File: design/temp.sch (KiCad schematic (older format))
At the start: 2 parts, among them U301 LM73

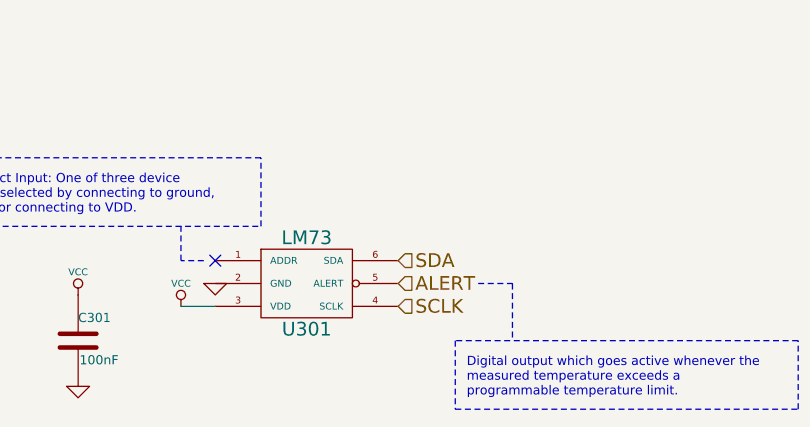
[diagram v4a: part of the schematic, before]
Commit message: Moved nRST cap closer to the MCU pin, connected crystal GND pins to the actual GND plane. Added several vias to GND and VDD planes.
Signed-off-by: Marcos Chaparro <marcos@mrkindustries.com.ar>
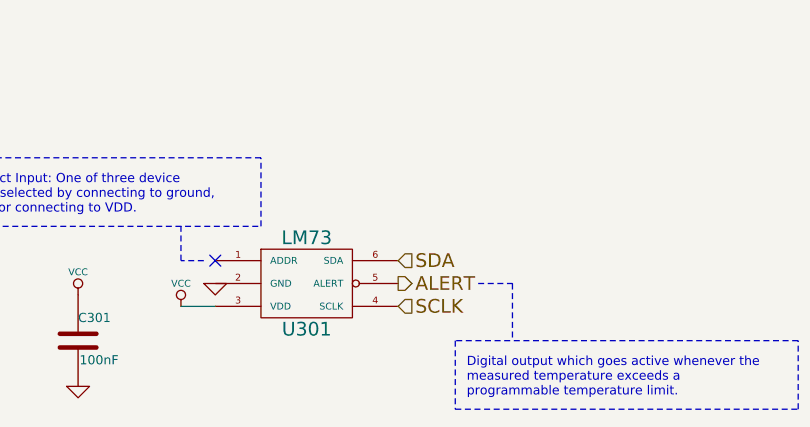
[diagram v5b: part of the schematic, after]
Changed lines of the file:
@@
 $EndComp
 $Comp
-L GND #PWR025
+L GND #PWR024
 U 1 1 53F5A7F7
 P 5400 3400
-F 0 "#PWR025" H 5400 3400 30  0001 C CNN
+F 0 "#PWR024" H 5400 3400 30  0001 C CNN
 F 1 "GND" H 5400 3330 30  0001 C CNN
 F 2 "" H 5400 3400 60  0000 C CNN
@@
 $EndComp
 $Comp
-L VCC #PWR026
+L VCC #PWR025
 U 1 1 53F5AB35
 P 5250 3500
-F 0 "#PWR026" H 5250 3600 30  0001 C CNN
+F 0 "#PWR025" H 5250 3600 30  0001 C CNN
 F 1 "VCC" H 5250 3600 30  0000 C CNN
 F 2 "" H 5250 3500 60  0001 C CNN
@@
 $EndComp
 $Comp
-L VCC #PWR027
+L VCC #PWR026
 U 1 1 53F5AB73
 P 4800 3450
-F 0 "#PWR027" H 4800 3550 30  0001 C CNN
+F 0 "#PWR026" H 4800 3550 30  0001 C CNN
 F 1 "VCC" H 4800 3550 30  0000 C CNN
 F 2 "" H 4800 3450 60  0001 C CNN
@@
 $EndComp
 $Comp
-L GND #PWR028
+L GND #PWR027
 U 1 1 53F5AB80
 P 4800 3850
-F 0 "#PWR028" H 4800 3850 30  0001 C CNN
+F 0 "#PWR027" H 4800 3850 30  0001 C CNN
 F 1 "GND" H 4800 3780 30  0001 C CNN
 F 2 "" H 4800 3850 60  0000 C CNN
@@
 Text HLabel 6200 3300 2    60   Input ~ 0
 SDA
-Text HLabel 6200 3400 2    60   Input ~ 0
+Text HLabel 6200 3400 2    60   Output ~ 0
 ALERT
 Text Notes 4100 3100 0    40   ~ 0
@@
 $Bitmap
 Pos 5600 4800
-Scale 1,000000
+Scale 1.000000
 Data
 89 50 4E 47 0D 0A 1A 0A 00 00 00 0D 49 48 44 52 00 00 02 6B 00 00 01 29 08 02 00 00 00 43 56 F2
@@
 $Bitmap
 Pos 3100 4000
-Scale 1,000000
+Scale 1.000000
 Data
 89 50 4E 47 0D 0A 1A 0A 00 00 00 0D 49 48 44 52 00 00 02 F0 00 00 01 AA 08 02 00 00 00 E2 39 E7
@@
 $Bitmap
 Pos 3200 5300
-Scale 1,000000
+Scale 1.000000
 Data
 89 50 4E 47 0D 0A 1A 0A 00 00 00 0D 49 48 44 52 00 00 03 4D 00 00 00 CE 08 02 00 00 00 6D AD 7E
@@
 41 E2 CF 04 72 F7 8E 04 09 12 24 48 90 20 41 E2 CF 09 D2 CF 23 41 82 04 09 12 24 48 90 F8 73 82
 F4 F3 48 90 20 41 82 04 09 12 24 FE 9C 20 FD 3C 12 24 48 90 20 41 82 04 89 3F 27 FE 1F 21 12 69
-2F 52 6F B5 AD 00 00 00 00 49 45 4E 44 AE 42 60 82 47
+2F 52 6F B5 AD 00 00 00 00 49 45 4E 44 AE 42 60 82 86
 EndData
 $EndBitmap
 $Bitmap
 Pos 7150 4850
-Scale 1,000000
+Scale 1.000000
 Data
 89 50 4E 47 0D 0A 1A 0A 00 00 00 0D 49 48 44 52 00 00 00 C8 00 00 00 C8 08 02 00 00 00 22 3A 39

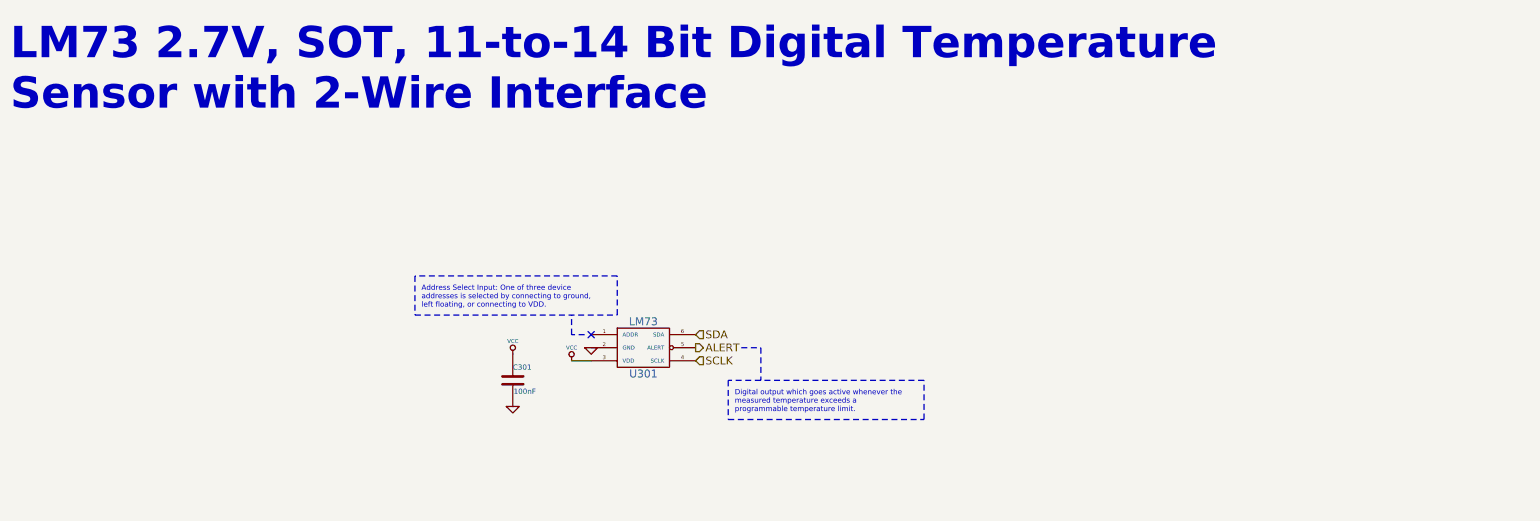
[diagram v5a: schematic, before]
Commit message: Changed i2c temperature sensor to NTC resistor to free the pins
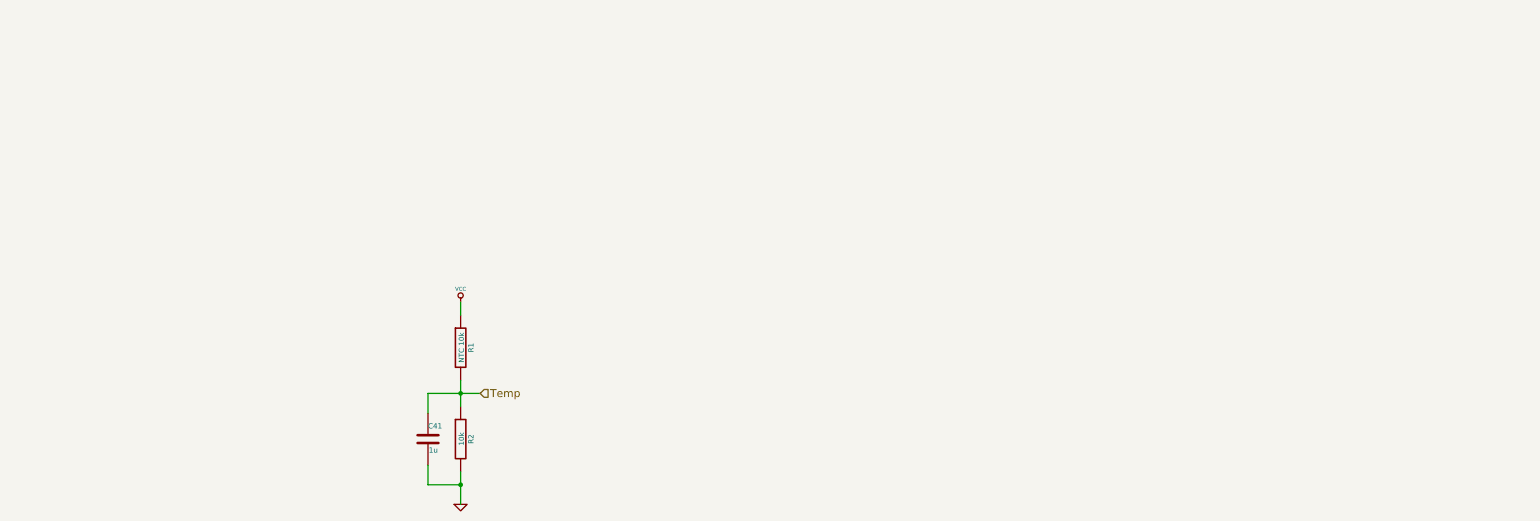
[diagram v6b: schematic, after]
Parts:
- removed C301: 100nF, SMD_Packages:SMD-0603, symbol C
- removed U301: LM73, SMD_Packages:SOT-23-6, symbol LM73
- added C41: 1u, SMD_Packages:SMD-0603_c, symbol C
- added R1: NTC 10k, SMD_Packages:SMD-0603_r, symbol R
- added R2: 10k, SMD_Packages:SMD-0603_r, symbol R
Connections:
- net GND: now also C41.2, R2.2
- net VCC: now also R1.1
- new net Temp: C41.1, R1.2, R2.1
- no-connect marks 1 -> 0
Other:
- note removed: "Address Select Input: One of three device\naddresses is selected by connecting to ground,\nleft floating, or connecting to VDD.\n"
- note removed: "Digital output which goes active whenever the\nmeasured temperature exceeds a\nprogrammable temperature limit."
- note removed: "LM73 2.7V, SOT, 11-to-14 Bit Digital Temperature\nSensor with 2-Wire Interface"

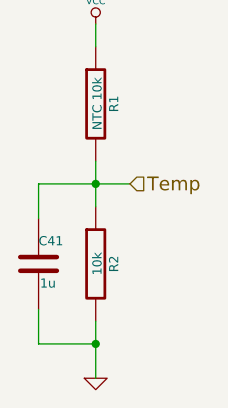
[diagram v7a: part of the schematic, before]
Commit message: Changed some capacitor values, made new assembly PDFs, added comment about R16 to schematic
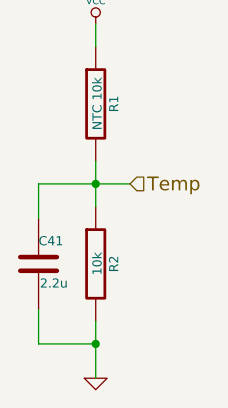
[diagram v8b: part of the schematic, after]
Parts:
- C41: value 1u -> 2.2u
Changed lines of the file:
@@
 P 4150 4100
 F 0 "C41" H 4150 4200 40  0000 L CNN
-F 1 "1u" H 4156 4015 40  0000 L CNN
+F 1 "2.2u" H 4156 4015 40  0000 L CNN
 F 2 "SMD_Packages:SMD-0603_c" H 4188 3950 30  0001 C CNN
 F 3 "" H 4150 4100 60  0000 C CNN
